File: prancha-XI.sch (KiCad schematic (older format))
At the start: 0 parts

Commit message: parte do esquemático da prancha 11 (essa prancha é cheia de truquezinhos de projeto e a notação é ambígua e aparentemente contém também diversos error no desenho. Vai ser um desafio interessante desvendar o significado de tudo isso...)
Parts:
- added 1B_P11, 5F_P11, U?: 74LS04, symbol 74LS04
- added 1C_P11, 1C_P? (x8), 5C_P11, U? (x2): 7400, symbol 7400
- added 2B_P11: 74LS107, symbol 74LS107
- added 3A_P11, U?: 74LS54, symbol 74LS54
- added 3A_P?, 3F_P11, 3F_P?, 4C_P11: 74LS10, ~, symbol 74LS10
- added U?: 7402, symbol 7402
- added U? (x3): 74LS20, symbol 74LS20
- added U?: 74LS30, symbol 74LS30
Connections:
- new net: 1B_P11.1, U?.8
- new net: 3A_P11.10, 5F_P11.4
- new net: 3A_P11.2, 3A_P11.4, 3A_P11.9, 5F_P11.2
- new net: 1B_P11.3, 3A_P11.8
- new net: 1B_P11.4, 2B_P11.1 (J)
- new net: 2B_P11.3 (Q), 3F_P11.11
- new net: 1B_P11.2, 2B_P11.4 (K)
- new net: 1B_P11.8, 1C_P11.2
- new net: 4C_P11.6, 5C_P11.9, U?.13
- new net: 3F_P11.8, 3F_P?.5
- new net: 1C_P11.4, 3F_P?.6
- new net: 1C_P11.11, 1C_P11.9
- new net: 1C_P11.12, 1C_P11.8
- new net: 1C_P?.1, 1C_P?.3 (x8)
- new net: 5C_P11.10, U?.3
- new net: 4C_P11.3, 5C_P11.8
- new net: 4C_P11.5, 5C_P11.11
- new net +ATIVO: 5F_P11.3
- new net +ESP: 1C_P11.1, 3A_P11.5
- new net +INT: U?.12
- new net +PAR: 3A_P11.3
- new net +RODA1: 2B_P11.2 (~Q)
- new net +T6: 2B_P11.12 (Cp)
- new net +T7: U?.10
- new net -(ESP.FORÇA_PUG): 1C_P11.3, 2B_P11.13 (Cd)
- new net -CF1: 5F_P11.1
- new net -FORÇA_PUG: 1B_P11.9, U?.8
- new net GND: 1B_P11.7 (GND), 1B_P11.7 (GND), 1B_P11.7 (GND), 1C_P11.7 (GND), 1C_P11.7 (GND), 1C_P11.7 (GND), 1C_P11.7 (GND), 1C_P?.7 (GND), 1C_P?.7 (GND), 1C_P?.7 (GND), 1C_P?.7 (GND), 1C_P?.7 (GND), 1C_P?.7 (GND), 1C_P?.7 (GND), 1C_P?.7 (GND), 2B_P11.7 (GND), 3A_P11.1, 3A_P11.7 (GND), 3A_P?.7 (GND), 3F_P11.7 (GND), 3F_P?.7 (GND), 4C_P11.7 (GND), 5C_P11.7 (GND), 5C_P11.7 (GND), 5F_P11.7 (GND), 5F_P11.7 (GND), U?.7 (GND), U?.7 (GND), U?.7 (GND), U?.7 (GND), U?.7 (GND), U?.7 (GND), U?.7 (GND), U?.7 (GND), U?.7 (GND)
- new net VCC: 1B_P11.14 (VCC), 1B_P11.14 (VCC), 1B_P11.14 (VCC), 1C_P11.14 (VCC), 1C_P11.14 (VCC), 1C_P11.14 (VCC), 1C_P11.14 (VCC), 1C_P?.14 (VCC), 1C_P?.14 (VCC), 1C_P?.14 (VCC), 1C_P?.14 (VCC), 1C_P?.14 (VCC), 1C_P?.14 (VCC), 1C_P?.14 (VCC), 1C_P?.14 (VCC), 2B_P11.14 (VCC), 3A_P11.14 (VCC), 3A_P?.14 (VCC), 3F_P11.14 (VCC), 3F_P?.14 (VCC), 4C_P11.14 (VCC), 5C_P11.14 (VCC), 5C_P11.14 (VCC), 5F_P11.14 (VCC), 5F_P11.14 (VCC), U?.14 (VCC), U?.14 (VCC), U?.14 (VCC), U?.14 (VCC), U?.14 (VCC), U?.14 (VCC), U?.14 (VCC), U?.14 (VCC), U?.14 (VCC)
- no-connect marks 0 -> 3
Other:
- note added: "(CF1.PAR) + (CF1.ESP) + (-ATIVO)"
- note added: "+CF1"
- note added: "+FORÇA_PUG"
- note added: "+RODA"
- note added: "-ATIVO"
- note added: "-RODA1"

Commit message: mais um pouco da prancha 11...
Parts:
- removed 1C_P? (x2), U?: 7400, symbol 7400
- removed 3A_P?: 74LS10, ~, symbol 74LS10
- removed U?: 7402, symbol 7402
- removed U?: 74LS04, symbol 74LS04
- removed U? (x2): 74LS20, symbol 74LS20
- removed U?: 74LS30, symbol 74LS30
- added 1B_P?, 3E_P11, U? (x2): 74LS04, symbol 74LS04
- added 1C_P? (x2), 2E_P11, U?: 7400, symbol 7400
- added 3A_P?, 4E_P11: 74LS10, ~, symbol 74LS10
- added unit 4 of 3C_P11
- added unit 2 of 3C_P11
- added unit 3 of 4C_P11
- added U? (x3): 7402, symbol 7402
- added U? (x2): 74LS20, symbol 74LS20
- added U?: 74LS30, symbol 74LS30
- gave numbers to parts that had none: 3
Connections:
- net +T6: now also 3C_P11.13, 3C_P11.5
- net GND: now also 1B_P?.7 (GND), 1C_P?.7 (GND), 1C_P?.7 (GND), 2E_P11.7 (GND), 2E_P11.7 (GND), 3A_P?.7 (GND), 3C_P11.7 (GND), 3C_P11.7 (GND), 3E_P11.7 (GND), 4C_P11.7 (GND), 4E_P11.7 (GND), U?.7 (GND), U?.7 (GND), U?.7 (GND), U?.7 (GND), U?.7 (GND), U?.7 (GND), U?.7 (GND), U?.7 (GND), U?.7 (GND)
- net VCC: now also 1B_P?.14 (VCC), 1C_P?.14 (VCC), 1C_P?.14 (VCC), 2E_P11.14 (VCC), 2E_P11.14 (VCC), 3A_P?.14 (VCC), 3C_P11.14 (VCC), 3C_P11.14 (VCC), 3E_P11.14 (VCC), 4C_P11.14 (VCC), 4E_P11.14 (VCC), U?.14 (VCC), U?.14 (VCC), U?.14 (VCC), U?.14 (VCC), U?.14 (VCC), U?.14 (VCC), U?.14 (VCC), U?.14 (VCC), U?.14 (VCC)
- net -LAL: now reaches 3F_P11.4
- net -LAL: now also 4C_P11.4, 4C_P11.11, 4E_P11.1
- net -RODA: now reaches 1C_P11.4, 3F_P11.6
- net -RODA: now also 1B_P?.1
- net +T5: now reaches 1C_P11.5
- net at 1C_P11.6: now also 1C_P11.13
- net at 1C_P11.12, 1C_P11.8: now also 1C_P?.1
- net -T1: now reaches 1C_P11.10
- net at 5C_P11.3: now also 4E_P11.13, U?.3
- net at 5C_P11.1: now also 4E_P11.12
- net at 5C_P11.2: now also 2E_P11.6
- net at 5C_P11.10: now also U?.6; no longer U?.3
- net at 4C_P11.3, 5C_P11.8: now also U?.2
- net pcb_15: now reaches 5C_P11.12
- net -INT: now reaches 5C_P11.13
- net -INT: now also 3C_P11.10
- new net: 3C_P11.8, 4C_P11.9, U?.5
- new net: 3C_P11.6, 3C_P11.9
- new net: 2E_P11.3, 4E_P11.2
- new net: 3C_P11.11, 4C_P11.10
- new net: U?.2, U?.3
- new net: 3C_P11.4, 3E_P11.2
- new net: 1C_P?.13, 1C_P?.3
- new net +FN: 1C_P?.2
- new net +INI: 2E_P11.4
- new net +PER: 2E_P11.1
- new net +PUL: 3C_P11.12
- new net +RODA: 1B_P?.2
- new net +T0: U?.4
- new net +T4: 2E_P11.2, 2E_P11.5
- new net -IMPEDE: U?.1, U?.1
- new net -PEDIDO_INTERRUPÇÃO: U?.2
- new net -T7: 1C_P?.12
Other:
- note added: "!!! (pinos errados)"
- note added: ""LIMPA AO LIGAR""
- note added: "+INIBE"
- note added: "+INT"
- note added: "+OCUPADO"
- note added: "-R"
- note added: "-S"
- note added: "11"
- note added: "13"
- note added: "CLOCK"
- moved on the sheet: 1B_P11D, 1C_P11A, 1C_P11B, 1C_P11C, 1C_P11D, 4C_P11B, 5C_P11A, 5C_P11C, 5C_P11D

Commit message: desenho parcial da prancha 11
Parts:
- removed 3A_P?: 74LS10, ~, symbol 74LS10
- removed U?: 7400, symbol 7400
- removed U?: 7402, symbol 7402
- removed U?: 74LS04, symbol 74LS04
- removed U? (x2): 74LS20, symbol 74LS20
- removed U?: 74LS30, symbol 74LS30
- added unit 3 of 1B_P11
- added unit 6 of 1B_P11
- added unit 3 of 1D_P11
- added 1D_P?, 5A_P11: 7402, symbol 7402
- added 1E_P11: 74LS107, symbol 74LS107
- added 2A_P11, 4E_P11: 74LS51, symbol 74LS51
- added unit 2 of 2B_P11
- added 2C_P11, 5D_P11: 74LS20, symbol 74LS20
- added 2D_P11, 3D_P11, 4B_P11, 4D_P11: 74HC74, symbol 74HC74
- added unit 4 of 2E_P11
- added unit 3 of 2E_P11
- added unit 6 of 3E_P11
- added unit 2 of 3E_P11
- added unit 3 of 3E_P11
- added unit 4 of 3E_P11
- added unit 5 of 3E_P11
- added 4A_P11: 7400, symbol 7400
- added unit 1 of 5B_P11
- added C? (x3): C, symbol C
- added D? (x2): DIODE, symbol DIODE
- added Q?: BC160, TO92, symbol BC413
- added R? (x6): R, symbol R
- added T?: THYRISTOR, symbol THYRISTOR
- gave numbers to parts that had none: 7
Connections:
- net +CF1: now also 4A_P11.5
- net +ESP: now also 1E_P11.3 (Q)
- net +PAR: now also 1E_P11.5 (Q)
- net +RODA: now also 1B_P11.10, 2C_P11.10, 2C_P11.4, 5B_P11.4, 5D_P11.10, 5D_P11.4; no longer 1B_P11.2
- net +T0: now also 4B_P11.3 (Cp)
- net +T4: now also 1E_P11.9 (Cp)
- net +T6: now also 2B_P11.9 (Cp), 4D_P11.11 (Cp)
- net -CF1: now also 1D_P11.9
- net -FORÇA_PUG: now also 2D_P11.1 (Cd), 3D_P11.4 (Sd)
- net -IMPEDE: now also 1D_P11.4, 5F_P11.5, 2A_P11.3, 2A_P11.5, 4A_P11.13; no longer 1D_P11.1, 5F_P11.1
- net -LAL: now also 2B_P11.10 (Cd)
- net -PEDIDO_INTERRUPÇÃO: now also 1D_P11.3; no longer 1D_P11.2
- net -RODA: now also 1B_P11.11; no longer 1B_P11.1
- net -T7: now also 1D_P?.2
- net GND: now also 1B_P11.7 (GND), 1B_P11.7 (GND), 1D_P11.7 (GND), 1D_P11.8, 1D_P?.7 (GND), 1E_P11.7 (GND), 1E_P11.7 (GND), 2A_P11.7 (GND), 2B_P11.7 (GND), 2C_P11.7 (GND), 2C_P11.7 (GND), 2D_P11.7 (GND), 2D_P11.7 (GND), 2E_P11.7 (GND), 2E_P11.7 (GND), 3D_P11.7 (GND), 3D_P11.7 (GND), 3E_P11.7 (GND), 3E_P11.7 (GND), 3E_P11.7 (GND), 3E_P11.7 (GND), 3E_P11.7 (GND), 4A_P11.7 (GND), 4A_P11.7 (GND), 4A_P11.7 (GND), 4A_P11.7 (GND), 4B_P11.7 (GND), 4B_P11.7 (GND), 4D_P11.7 (GND), 4D_P11.7 (GND), 4E_P11.7 (GND), 5A_P11.7 (GND), 5A_P11.7 (GND), 5B_P11.7 (GND), 5D_P11.7 (GND), 5D_P11.7 (GND), C?.1, Q?.3 (E), R?.1, R?.1, T?.K
- net VCC: now also 1B_P11.14 (VCC), 1B_P11.14 (VCC), 1D_P11.14 (VCC), 1D_P?.14 (VCC), 1E_P11.14 (VCC), 1E_P11.14 (VCC), 2A_P11.14 (VCC), 2B_P11.14 (VCC), 2C_P11.14 (VCC), 2C_P11.14 (VCC), 2D_P11.14 (VCC), 2D_P11.14 (VCC), 2E_P11.12, 2E_P11.14 (VCC), 2E_P11.14 (VCC), 3D_P11.14 (VCC), 3D_P11.14 (VCC), 3E_P11.14 (VCC), 3E_P11.14 (VCC), 3E_P11.14 (VCC), 3E_P11.14 (VCC), 3E_P11.14 (VCC), 4A_P11.14 (VCC), 4A_P11.14 (VCC), 4A_P11.14 (VCC), 4A_P11.14 (VCC), 4B_P11.14 (VCC), 4B_P11.14 (VCC), 4D_P11.14 (VCC), 4D_P11.14 (VCC), 4E_P11.14 (VCC), 5A_P11.14 (VCC), 5A_P11.14 (VCC), 5B_P11.14 (VCC), 5D_P11.14 (VCC), 5D_P11.14 (VCC)
- net at 3F_P11.10: now also 4A_P11.8
- net at 3F_P11.9: now also 2B_P11.6 (~Q)
- net at 3B_P11.1: now also 3B_P11.11; no longer 3B_P11.3
- net -(BOT-PART-A): now reaches 3B_P11.2
- net at 3B_P11.3: now also 3B_P11.13, 4B_P11.2 (D), D?.1 (A); no longer 3B_P11.1
- net at 4E_P11.13, 5C_P11.3: now also 1D_P11.6; no longer 1D_P11.3
- net at 4C_P11.3, 5C_P11.8: now also 1D_P11.5; no longer 1D_P11.2
- net CLOCK: now reaches 1D_P11.11
- net CLOCK: now also 2D_P11.11 (Cp), 2D_P11.3 (Cp), 3D_P11.11 (Cp), 3D_P11.3 (Cp), 4D_P11.3 (Cp)
- new net: 3B_P11.5, 3B_P11.8
- new net: 2A_P11.2, 3B_P11.6, 3B_P11.9
- new net: 2D_P11.5 (Q), 5D_P11.2
- new net: 2D_P11.12 (D), 3E_P11.12
- new net: 2D_P11.9 (Q), 5D_P11.12
- new net: 1D_P11.10, 2D_P11.2 (D)
- new net: 2E_P11.11, 3D_P11.2 (D)
- new net: 2C_P11.2, 3D_P11.5 (Q)
- new net: 3D_P11.12 (D), 3E_P11.4
- new net: 2C_P11.12, 3D_P11.9 (Q)
- new net: 3E_P11.6, 4D_P11.2 (D)
- new net: 4D_P11.5 (Q), 5B_P11.2
- new net: 1D_P11.2, 5F_P11.6
- new net: 2E_P11.9, 4B_P11.12 (D), 4B_P11.5 (Q)
- new net: 4B_P11.6 (~Q), 4E_P11.4, 4E_P11.5, 5A_P11.5
- new net: 1D_P?.1, 4B_P11.11 (Cp)
- new net: 2E_P11.10, 4B_P11.8 (~Q)
- new net: 4B_P11.9 (Q), 4E_P11.2, 4E_P11.3, 5A_P11.6
- new net: 3E_P11.9, 5A_P11.4
- new net: 1B_P11.12, 2B_P11.11 (K)
- new net: 1B_P11.6, 2B_P11.8 (J)
- new net: 1B_P11.5, 4A_P11.3
- new net: 1B_P11.13, 4A_P11.6
- new net: 4A_P11.12, 4D_P11.9 (Q), 5A_P11.11
- new net: C?.1, R?.2, R?.2, T?.G
- new net: D?.1 (A), R?.1
- new net: C?.1, D?.2 (K), Q?.2 (B), R?.2
- new net: 1E_P11.4 (K), 4A_P11.11
- new net: 1E_P11.11 (K), 5A_P11.13
- new net: C?.2, D?.2 (K), R?.1
- new net: 2A_P11.6, 3E_P11.11
- new net: 1E_P11.1 (J), 3E_P11.10
- new net: Q?.1 (C), R?.1
- new net +CLOCK: 1D_P?.3
- new net +CS: 4A_P11.10
- new net +ESP-D: 2A_P11.4
- new net +IS: 4A_P11.2
- new net +PAR-D: 1E_P11.8 (J)
- new net +PARTIDA: 4A_P11.1, 4A_P11.9
- new net +PARTIDA2: 4E_P11.6
- new net -(BOT-ESP-A): 3B_P11.4
- new net -(BOT-ESP-N): 3B_P11.10
- new net -(BOT-PART-N): 3B_P11.12
- new net -ATIVO: 4A_P11.4, 5A_P11.12
- new net -CF2: 3E_P11.13
- new net -CF3: 2E_P11.13
- new net -CF4: 3E_P11.3
- new net -CF5: 3E_P11.5
- new net -ESP: 1E_P11.2 (~Q)
- new net -F1: 5D_P11.6
- new net -F1-D: 2D_P11.6 (~Q)
- new net -F2: 5D_P11.8
- new net -F2-D: 2D_P11.8 (~Q)
- new net -F3: 2C_P11.6
- new net -F3-D: 3D_P11.6 (~Q)
- new net -F4: 2C_P11.8
- new net -F4-D: 3D_P11.8 (~Q)
- new net -F5: 5B_P11.6
- new net -F5-D: 4D_P11.6 (~Q)
- new net -LAL3: 2D_P11.13 (Cd), 2D_P11.4 (Sd), 3D_P11.1 (Cd), 3D_P11.13 (Cd), 4D_P11.1 (Cd)
- new net -PAR: 1E_P11.6 (~Q)
- new net -PARTIDA: 3E_P11.8, 4D_P11.12 (D)
- new net -PARTIDA2: 2E_P11.8
- new net -PRESET: C?.2, C?.2, R?.2, R?.2, T?.A
- new net -T3: 1E_P11.12 (Cp)
- no-connect marks 3 -> 26
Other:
- note added: "!!! (erro no esquemático?)"
- note added: "(NOR)"
- note added: "(NOT)"
- note added: "-PARTIDA-ATRASADA"
- note added: "-RODA3"
- note added: "???"
- note removed: "CLOCK"
- moved on the sheet: 1B_P11A, 1B_P11B, 1B_P11D, 1C_P11A, 1C_P11B, 1C_P11C, 1C_P11D, 1D_P11A, 1D_P11D, 2B_P11A, 2E_P11A, 2E_P11B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

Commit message: conector de 70 pinos para a interconexão das placas e término do desenho da prancha 5.
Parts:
- added 4F_P11: 74LS04, symbol 74LS04
- added P?: CONN_35X2, symbol CONN_35X2
- added U? (x2): 74LS51, symbol 74LS51
- added U?: 74LS55, symbol 74LS55
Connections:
- net +PARTIDA2: now also 4E_P11.9; no longer 4E_P11.6
- net -LAL: now also 4F_P11.12
- net -LAL3: now also 4F_P11.10
- net GND: now also 4F_P11.7 (GND), 4F_P11.7 (GND), 4F_P11.7 (GND), 4F_P11.7 (GND), 4F_P11.7 (GND), 4F_P11.7 (GND), U?.7 (GND), U?.7 (GND), U?.7 (GND)
- net VCC: now also R?.1, R?.2, 4F_P11.14 (VCC), 4F_P11.14 (VCC), 4F_P11.14 (VCC), 4F_P11.14 (VCC), 4F_P11.14 (VCC), 4F_P11.14 (VCC), U?.14 (VCC), U?.14 (VCC), U?.14 (VCC)
- net at 4B_P11.6 (~Q), 5A_P11.5: now also 4E_P11.12, 4E_P11.13; no longer 4E_P11.4, 4E_P11.5
- net at 4B_P11.9 (Q), 5A_P11.6: now also 4E_P11.1, 4E_P11.10; no longer 4E_P11.2, 4E_P11.3
- net at Q?.1 (C), R?.1: now also 4F_P11.1
- new net: 4F_P11.11, 4F_P11.13, 4F_P11.2, 4F_P11.3, 4F_P11.5, 4F_P11.9
- new net -LAL1: 4F_P11.4
- new net -LAL2: 4F_P11.6
- new net -LAL4: 4F_P11.8
- new net ?: P?.1 (P1), P?.10 (P10), P?.11 (P11), P?.12 (P12), P?.13 (P13), P?.14 (P14), P?.15 (P15), P?.16 (P16), P?.17 (P17), P?.18 (P18), P?.19 (P19), P?.2 (P2), P?.20 (P20), P?.21 (P21), P?.22 (P22), P?.23 (P23), P?.24 (P24), P?.25, P?.26 (P26), P?.27 (P27), P?.28 (P28), P?.29 (P29), P?.3 (P3), P?.30 (P30), P?.31 (P31), P?.32 (P32), P?.33 (P33), P?.34 (P34), P?.35 (P35), P?.36 (P36), P?.37 (P37), P?.38 (P38), P?.39 (P39), P?.4 (P4), P?.40 (P40), P?.41 (P41), P?.42 (P42), P?.43 (P43), P?.44 (P44), P?.45 (P45), P?.46 (P46), P?.47 (P47), P?.48 (P48), P?.49 (P49), P?.5 (P5), P?.50 (P50), P?.51 (P51), P?.52 (P52), P?.53 (P53), P?.54 (P54), P?.55 (P55), P?.56 (P56), P?.57 (P57), P?.58 (P58), P?.59 (P59), P?.6 (P6), P?.60 (P60), P?.61 (P61), P?.62 (P62), P?.63 (P63), P?.64 (P64), P?.65 (P65), P?.66 (P66), P?.67 (P67), P?.68 (P68), P?.69 (P69), P?.7 (P7), P?.70 (P70), P?.8 (P8), P?.9 (P9)
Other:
- moved on the sheet: 1B_P11A, 1B_P11B, 1B_P11C, 1B_P11D, 1B_P11E, 1B_P11F, 1C_P11A, 1C_P11B, 1C_P11C, 1C_P11D, 1D_P11A, 1D_P11B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

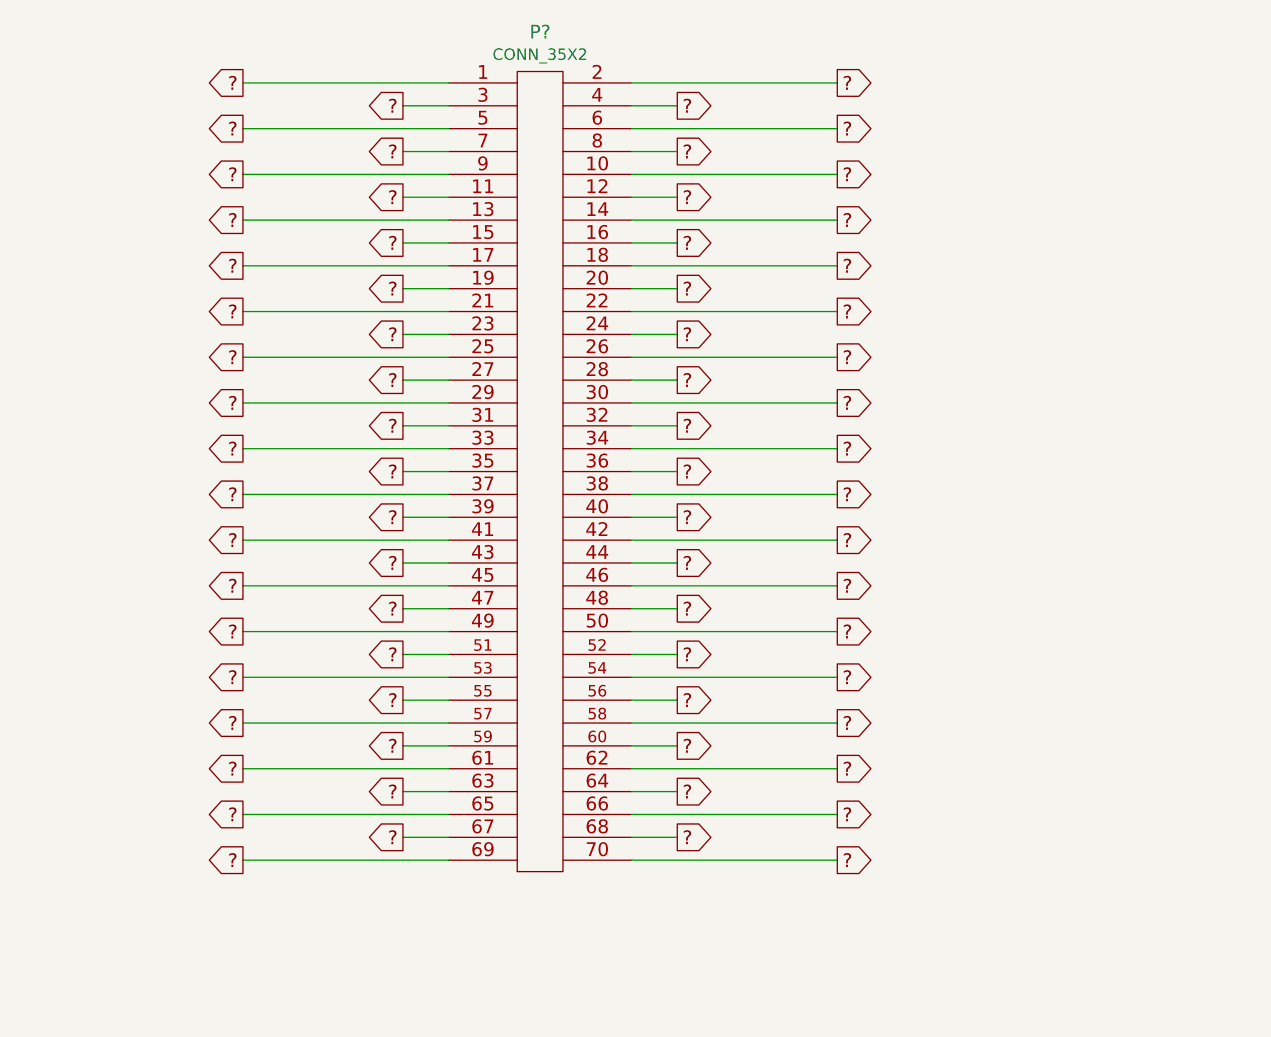
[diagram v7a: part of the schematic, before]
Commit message: vários trechos de transcrição e, em particular, término do conector dos sinais da prancha 11.
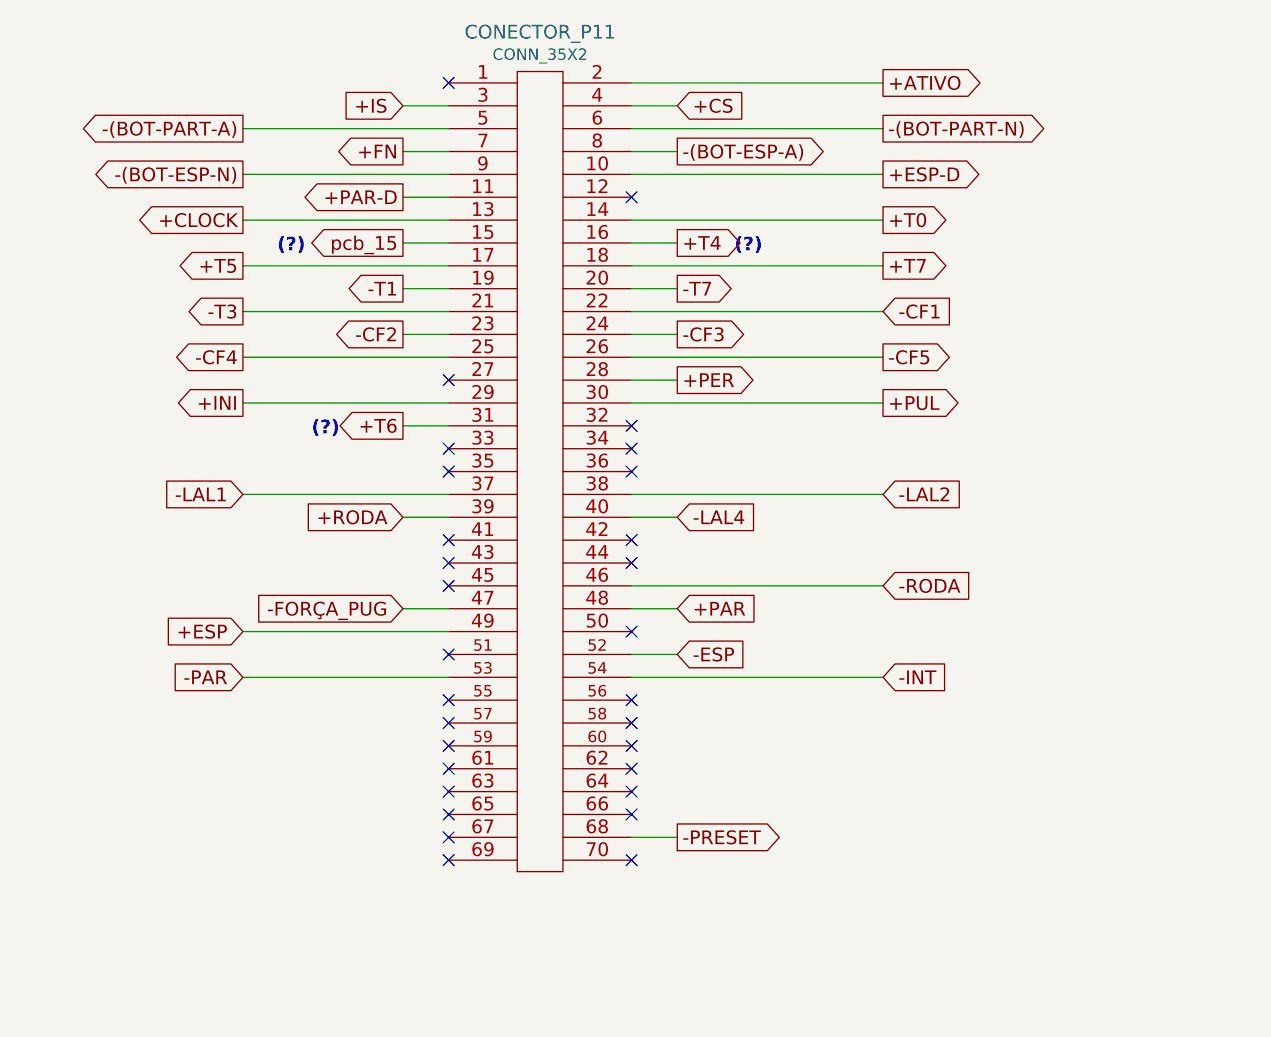
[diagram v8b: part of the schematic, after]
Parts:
- gave numbers to parts that had none: 1
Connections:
- net +ATIVO: now also CONECTOR_P11.2 (P2)
- net +CLOCK: now also CONECTOR_P11.13 (P13)
- net +CS: now also CONECTOR_P11.4 (P4)
- net +ESP: now also CONECTOR_P11.49 (P49)
- net +ESP-D: now also CONECTOR_P11.10 (P10)
- net +FN: now also CONECTOR_P11.7 (P7)
- net +INI: now also CONECTOR_P11.29 (P29)
- net +IS: now also CONECTOR_P11.3 (P3)
- net +PAR: now also CONECTOR_P11.48 (P48)
- net +PAR-D: now also CONECTOR_P11.11 (P11)
- net +PER: now also CONECTOR_P11.28 (P28)
- net +PUL: now also CONECTOR_P11.30 (P30)
- net +RODA: now also CONECTOR_P11.39 (P39)
- net +T0: now also CONECTOR_P11.14 (P14)
- net +T4: now also CONECTOR_P11.16 (P16)
- net +T5: now also CONECTOR_P11.17 (P17)
- net +T6: now also CONECTOR_P11.31 (P31)
- net +T7: now also CONECTOR_P11.18 (P18)
- net -(BOT-ESP-A): now also CONECTOR_P11.8 (P8)
- net -(BOT-ESP-N): now also CONECTOR_P11.9 (P9)
- net -(BOT-PART-A): now also CONECTOR_P11.5 (P5)
- net -(BOT-PART-N): now also CONECTOR_P11.6 (P6)
- net -CF1: now also CONECTOR_P11.22 (P22)
- net -CF2: now also CONECTOR_P11.23 (P23)
- net -CF3: now also CONECTOR_P11.24 (P24)
- net -CF4: now also CONECTOR_P11.25
- net -CF5: now also CONECTOR_P11.26 (P26)
- net -ESP: now also CONECTOR_P11.52 (P52)
- net -FORÇA_PUG: now also CONECTOR_P11.47 (P47)
- net -INT: now also CONECTOR_P11.54 (P54)
- net -LAL1: now also CONECTOR_P11.37 (P37)
- net -LAL2: now also CONECTOR_P11.38 (P38)
- net -LAL4: now also CONECTOR_P11.40 (P40)
- net -PAR: now also CONECTOR_P11.53 (P53)
- net -PRESET: now also CONECTOR_P11.68 (P68)
- net -RODA: now also CONECTOR_P11.46 (P46)
- net -T1: now also CONECTOR_P11.19 (P19)
- net -T3: now also CONECTOR_P11.21 (P21)
- net -T7: now also CONECTOR_P11.20 (P20)
- net pcb_15: now also CONECTOR_P11.15 (P15)
- removed net ?: CONECTOR_P11.1 (P1), CONECTOR_P11.10 (P10), CONECTOR_P11.11 (P11), CONECTOR_P11.12 (P12), CONECTOR_P11.13 (P13), CONECTOR_P11.14 (P14), CONECTOR_P11.15 (P15), CONECTOR_P11.16 (P16), CONECTOR_P11.17 (P17), CONECTOR_P11.18 (P18), CONECTOR_P11.19 (P19), CONECTOR_P11.2 (P2), CONECTOR_P11.20 (P20), CONECTOR_P11.21 (P21), CONECTOR_P11.22 (P22), CONECTOR_P11.23 (P23), CONECTOR_P11.24 (P24), CONECTOR_P11.25, CONECTOR_P11.26 (P26), CONECTOR_P11.27 (P27), CONECTOR_P11.28 (P28), CONECTOR_P11.29 (P29), CONECTOR_P11.3 (P3), CONECTOR_P11.30 (P30), CONECTOR_P11.31 (P31), CONECTOR_P11.32 (P32), CONECTOR_P11.33 (P33), CONECTOR_P11.34 (P34), CONECTOR_P11.35 (P35), CONECTOR_P11.36 (P36), CONECTOR_P11.37 (P37), CONECTOR_P11.38 (P38), CONECTOR_P11.39 (P39), CONECTOR_P11.4 (P4), CONECTOR_P11.40 (P40), CONECTOR_P11.41 (P41), CONECTOR_P11.42 (P42), CONECTOR_P11.43 (P43), CONECTOR_P11.44 (P44), CONECTOR_P11.45 (P45), CONECTOR_P11.46 (P46), CONECTOR_P11.47 (P47), CONECTOR_P11.48 (P48), CONECTOR_P11.49 (P49), CONECTOR_P11.5 (P5), CONECTOR_P11.50 (P50), CONECTOR_P11.51 (P51), CONECTOR_P11.52 (P52), CONECTOR_P11.53 (P53), CONECTOR_P11.54 (P54), CONECTOR_P11.55 (P55), CONECTOR_P11.56 (P56), CONECTOR_P11.57 (P57), CONECTOR_P11.58 (P58), CONECTOR_P11.59 (P59), CONECTOR_P11.6 (P6), CONECTOR_P11.60 (P60), CONECTOR_P11.61 (P61), CONECTOR_P11.62 (P62), CONECTOR_P11.63 (P63), CONECTOR_P11.64 (P64), CONECTOR_P11.65 (P65), CONECTOR_P11.66 (P66), CONECTOR_P11.67 (P67), CONECTOR_P11.68 (P68), CONECTOR_P11.69 (P69), CONECTOR_P11.7 (P7), CONECTOR_P11.70 (P70), CONECTOR_P11.8 (P8), CONECTOR_P11.9 (P9)
- no-connect marks 26 -> 56
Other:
- note added: "(?)"
